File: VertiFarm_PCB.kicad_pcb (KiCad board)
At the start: 4 copper layers, 210 x 107 mm, 80 parts, among them J1 Peltier, J10 Raspberry Pi 5, J11 Peltier, J13 3V3 I2C, J15 3V3 I2C, J17 3V3 I2C, J18 5V I2C, J19 3V3 I2C, J2 FAN 1, J20 Switch_2, J21 Camera, J22 DS12B20, J23 DS12B20, J24 DS12B20, J25 DS12B20, J26 DHT22, J27 DHT22, J3 FAN 2, J33 left, J34 right, J35 LED 1, J36 LED 2, J4 FAN 3, J5 Switch_1, J6 FAN 4, J7 PCIe Header, J8 4 Pin Molex Header, J9 5V I2C, Q1 IRLZ44N, Q2 IRLZ44N, Q3 IRLZ44N, U1 ESP32-DEVKITC-32E, U2 TC4427CPA, U3 TC4427CPA, U4 TC4427CPA, U5 TC4427CPA

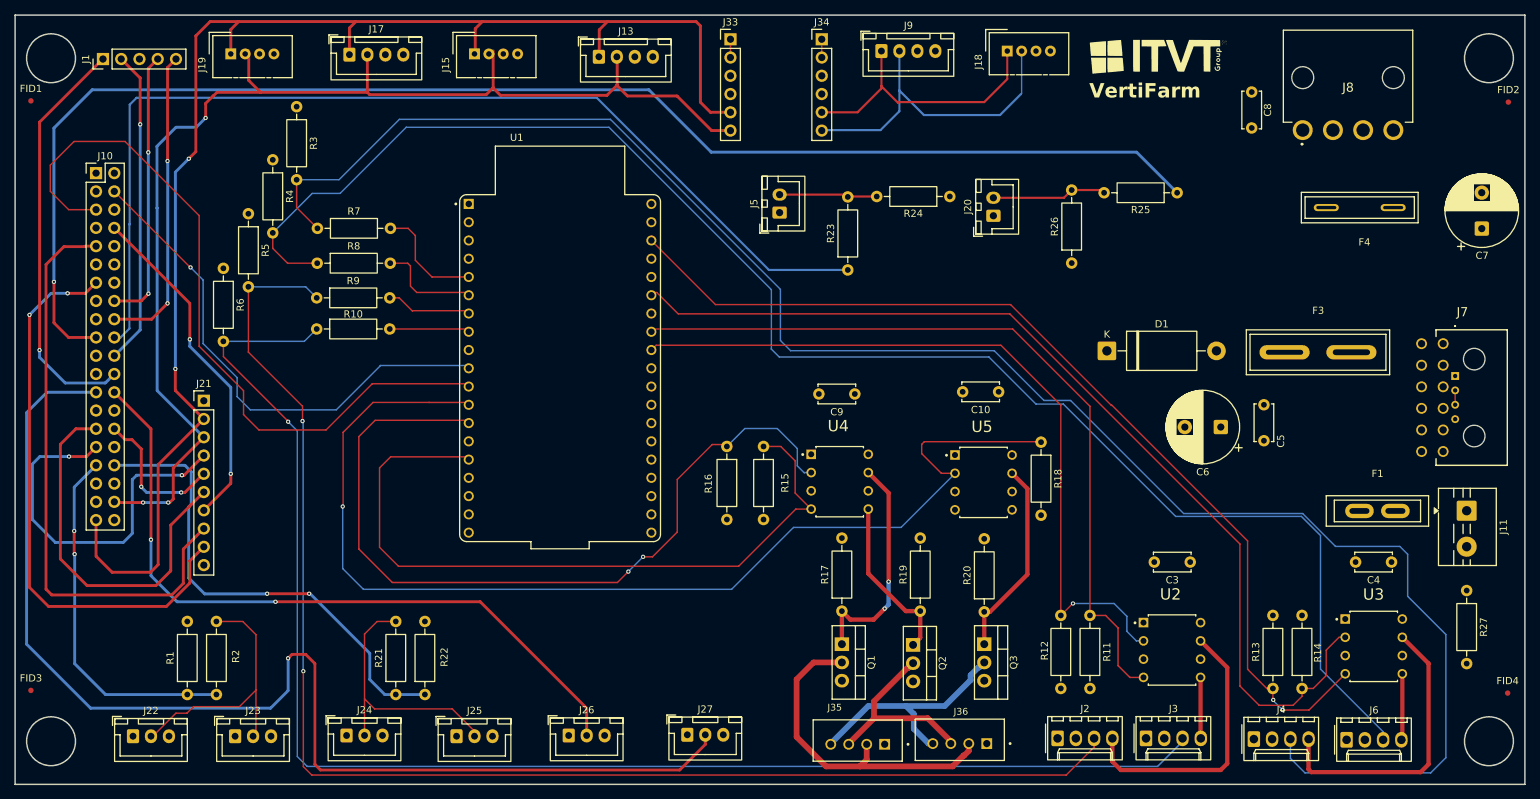
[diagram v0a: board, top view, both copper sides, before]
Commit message: Rpi pinouts corrected
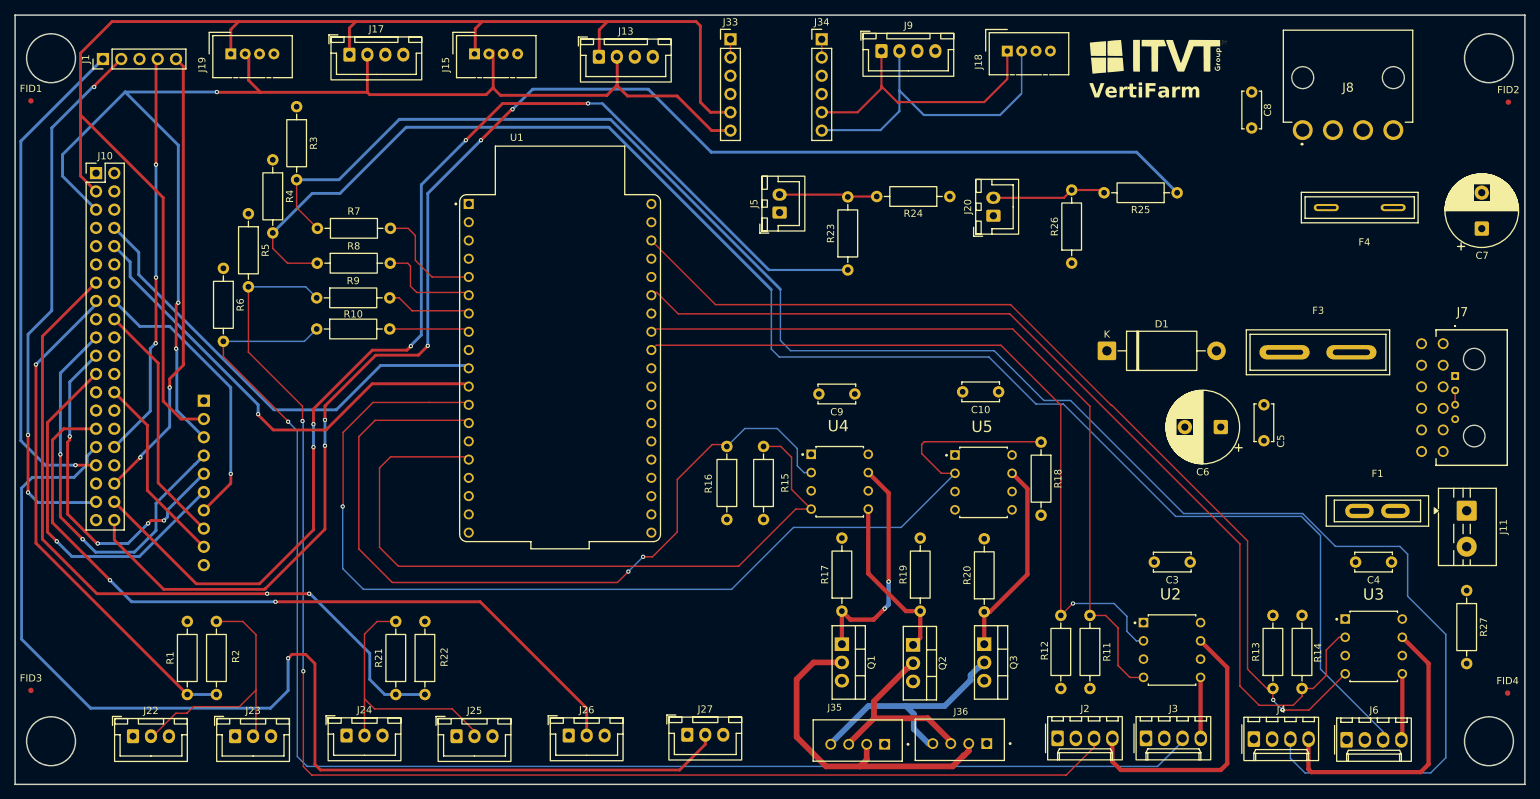
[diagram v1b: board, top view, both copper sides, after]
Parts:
- J21: moved to B.Cu
- turned J21 to 180 degrees
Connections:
- J10 pad 1: unconnected-(J10-Pin_1-Pad1) -> 3V3
- J10 pad 10: unconnected-(J10-Pin_10-Pad10) -> GPIO 15
- J10 pad 13: GPIO 7 -> GPIO 27
- J10 pad 15: unconnected-(J10-Pin_15-Pad15) -> GPIO 22
- J10 pad 16: GPIO 12 -> GPIO 23
- J10 pad 18: GPIO 16 -> GPIO 24
- J10 pad 19: GPIO 21 -> GPIO 10
- J10 pad 20: GPIO 20 -> unconnected-(J10-Pin_20-Pad20)
- J10 pad 21: GND -> GPIO 9
- J10 pad 22: GPIO 26 -> unconnected-(J10-Pin_22-Pad22)
- J10 pad 23: unconnected-(J10-Pin_23-Pad23) -> GPIO 11
- J10 pad 24: GPIO 13 -> unconnected-(J10-Pin_24-Pad24)
- J10 pad 25: GPIO 6 -> unconnected-(J10-Pin_25-Pad25)
- J10 pad 26: GPIO 5 -> GPIO 7
- J10 pad 29: GPIO 11 -> GPIO 5
- J10 pad 3: unconnected-(J10-Pin_3-Pad3) -> GPIO 2
- J10 pad 30: GPIO 9 -> unconnected-(J10-Pin_30-Pad30)
- J10 pad 31: GPIO 10 -> GPIO 6
- J10 pad 32: unconnected-(J10-Pin_32-Pad32) -> GPIO 12
- J10 pad 33: GPIO 22 -> GPIO 13
- J10 pad 34: GPIO 27 -> unconnected-(J10-Pin_34-Pad34)
- J10 pad 36: GND -> GPIO 16
- J10 pad 37: unconnected-(J10-Pin_37-Pad37) -> GPIO 26
- J10 pad 38: GPIO 3 -> GPIO 20
- J10 pad 39: GPIO 2 -> unconnected-(J10-Pin_39-Pad39)
- J10 pad 4: GPIO 14 -> unconnected-(J10-Pin_4-Pad4)
- J10 pad 40: 3V3 -> GPIO 21
- J10 pad 5: GPIO 15 -> GPIO 3
- J10 pad 8: GPIO 23 -> GPIO 14
- J10 pad 9: GPIO 24 -> GND
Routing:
- net GPIO 7: track 79.6 -> 26.7 mm, vias 2 -> 0
- net GPIO 24: track 82.1 -> 34.3 mm
- net GPIO 15: track 102.7 -> 65.3 mm, vias 0 -> 1
- net GPIO 27: track 67.7 -> 103.1 mm
- net GPIO 26: track 43.9 -> 75.9 mm, vias 1 -> 3
- net GPIO 9: track 20.3 -> 48.9 mm, vias 2 -> 4
- net GPIO 20: track 144.0 -> 166.2 mm, vias 0 -> 5
- net GPIO 16: track 42.8 -> 63.4 mm
- net GPIO 22: track 50.4 -> 71.0 mm, vias 2 -> 1
- net GPIO 12: track 38.4 -> 56.5 mm, vias 2 -> 3
- net GPIO 3: track 171.1 -> 184.0 mm
- net GPIO 21: track 198.2 -> 210.7 mm, vias 1 -> 5
- net GPIO 13: track 57.6 -> 69.7 mm
- net GPIO 23: track 47.5 -> 39.8 mm, vias 2 -> 1
- net GPIO 6: track 164.6 -> 157.2 mm
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
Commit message: Updated the Fuses Footprints and Corrected Layout
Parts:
- F1: footprint Fuse_Blade:Fuse_Blade_ATO_directSolder_32V_15A -> Footprint:Fuse_Blade_ATO_directSolder_32V_15A
- F3: footprint Fuse_Blade:Fuse_Blade_ATO_directSolder_32V_40A -> Footprint:Fuse_Blade_ATO_directSolder_32V_40A
- F4: footprint Fuse_Blade:Fuse_Blade_ATO_12VDC_10A -> Footprint:Fuse_Blade_ATO_12VDC_10A
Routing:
- net GPIO 2: track 195.3 -> 198.0 mm
- net GPIO 20: track 166.2 -> 167.0 mm
- net GPIO 15: track 65.3 -> 65.9 mm
- net GPIO 21: track 210.7 -> 211.2 mm
- net GPIO 27: vias 2 -> 1

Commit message: Corrected Layout
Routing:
- net GPIO 15: track 65.9 -> 62.9 mm, vias 1 -> 0
- net GPIO 3: track 183.7 -> 183.1 mm
- net GPIO 20: track 167.0 -> 166.9 mm, vias 5 -> 3
- net GPIO 21: vias 5 -> 3

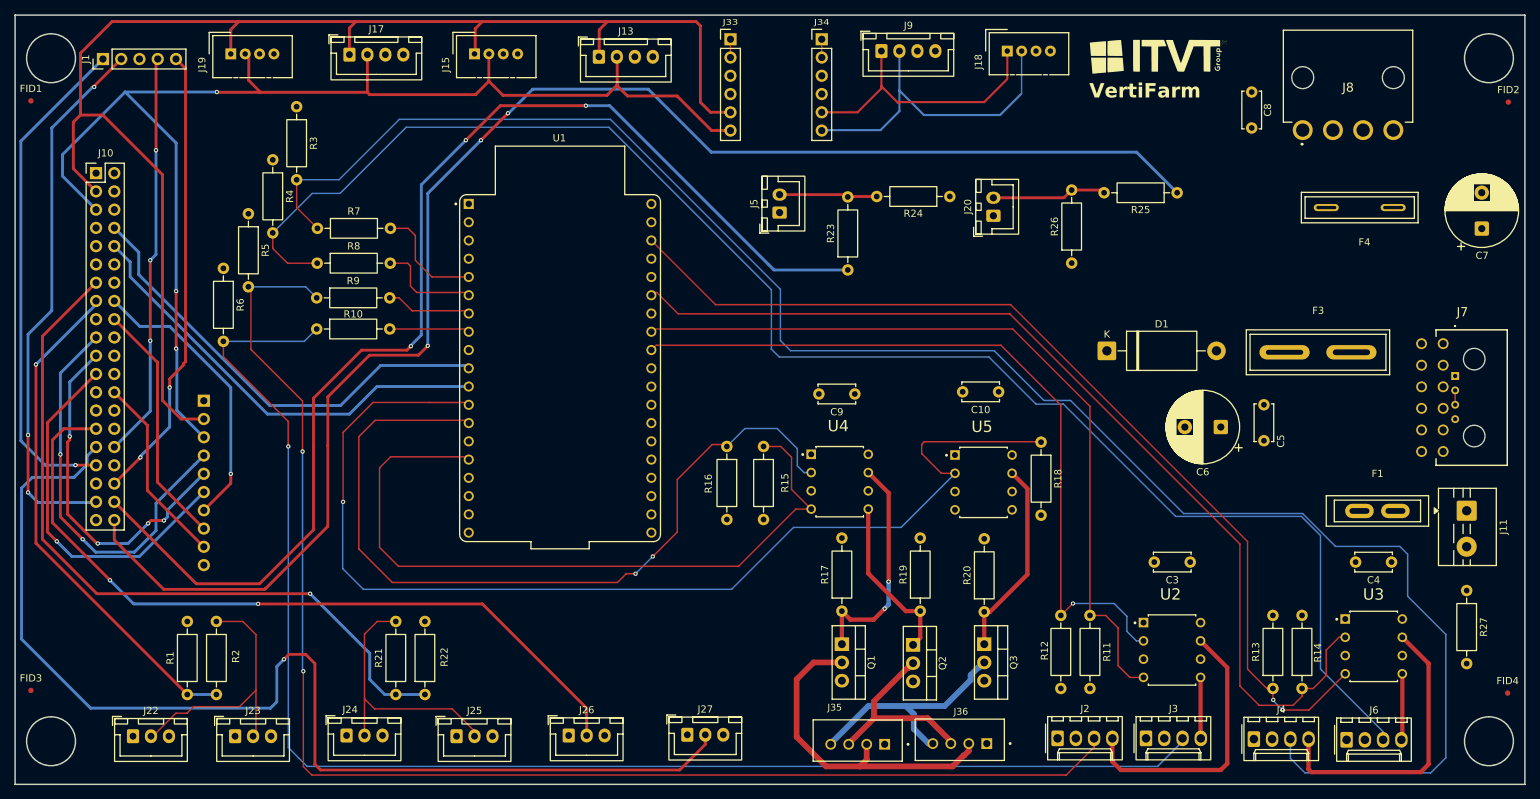
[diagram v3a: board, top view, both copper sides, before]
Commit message: updated the connector pins
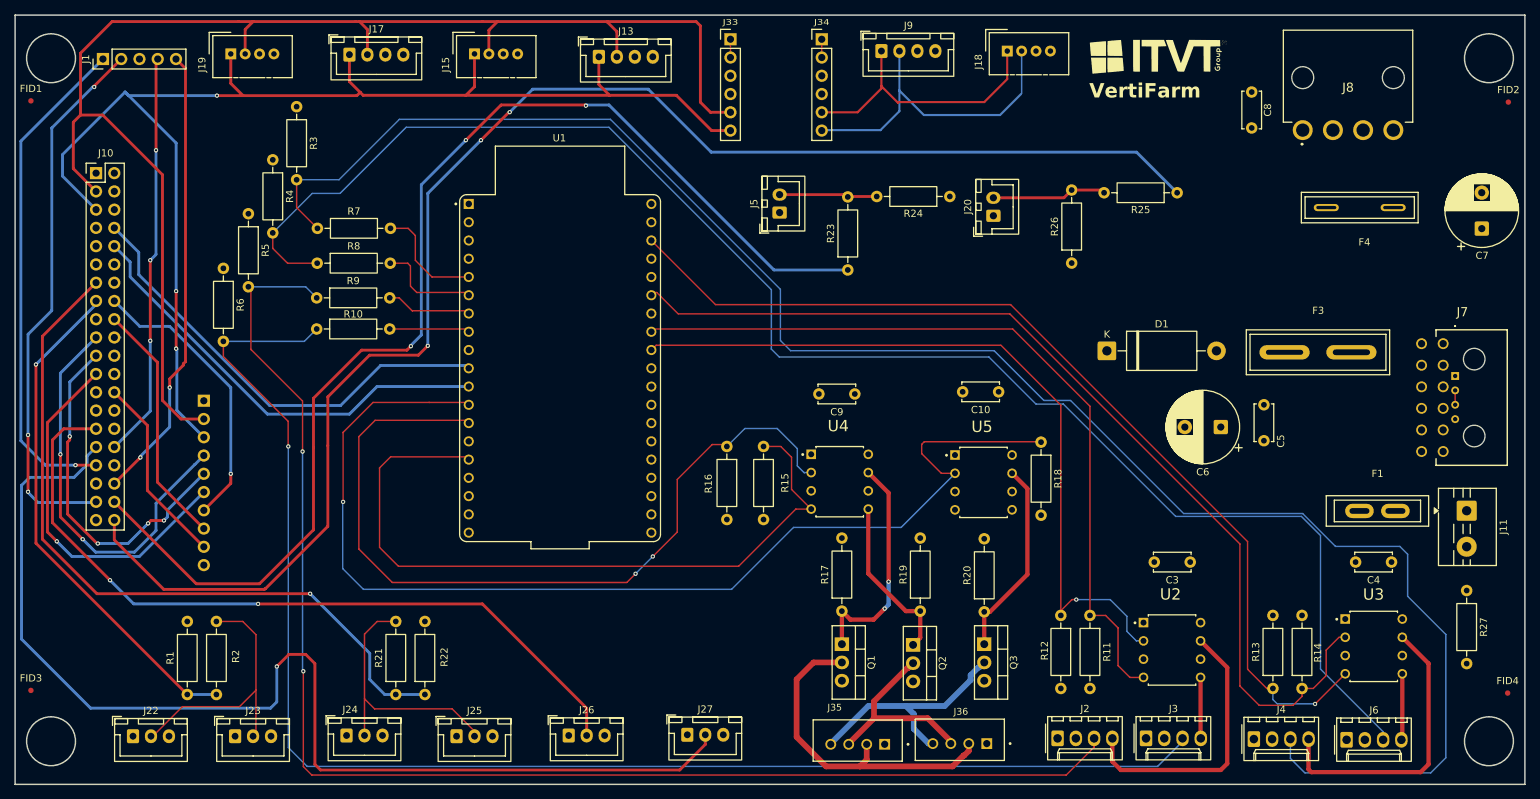
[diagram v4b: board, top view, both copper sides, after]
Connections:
- J13 pad 1: GPIO 2 -> GPIO 3
- J13 pad 2: GPIO 3 -> GPIO 2
- J15 pad 1: GPIO 2 -> GPIO 3
- J15 pad 2: GPIO 3 -> GPIO 2
- J17 pad 1: GPIO 2 -> GPIO 3
- J17 pad 2: GPIO 3 -> GPIO 2
- J19 pad 1: GPIO 2 -> GPIO 3
- J19 pad 2: GPIO 3 -> GPIO 2
- J21 pad 2: GPIO 2 -> GPIO 3
- J21 pad 3: GPIO 3 -> GPIO 2
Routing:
- net GPIO 3: track 183.1 -> 186.1 mm
- net 3V3: track 362.2 -> 361.2 mm
- net IO 18: track 105.5 -> 106.3 mm
- net IO 22: track 137.0 -> 136.3 mm, vias 2 -> 1
